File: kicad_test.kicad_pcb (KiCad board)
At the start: 2 copper layers, 10 parts, among them U1 ICM7555xP, U2 ICM7555xP

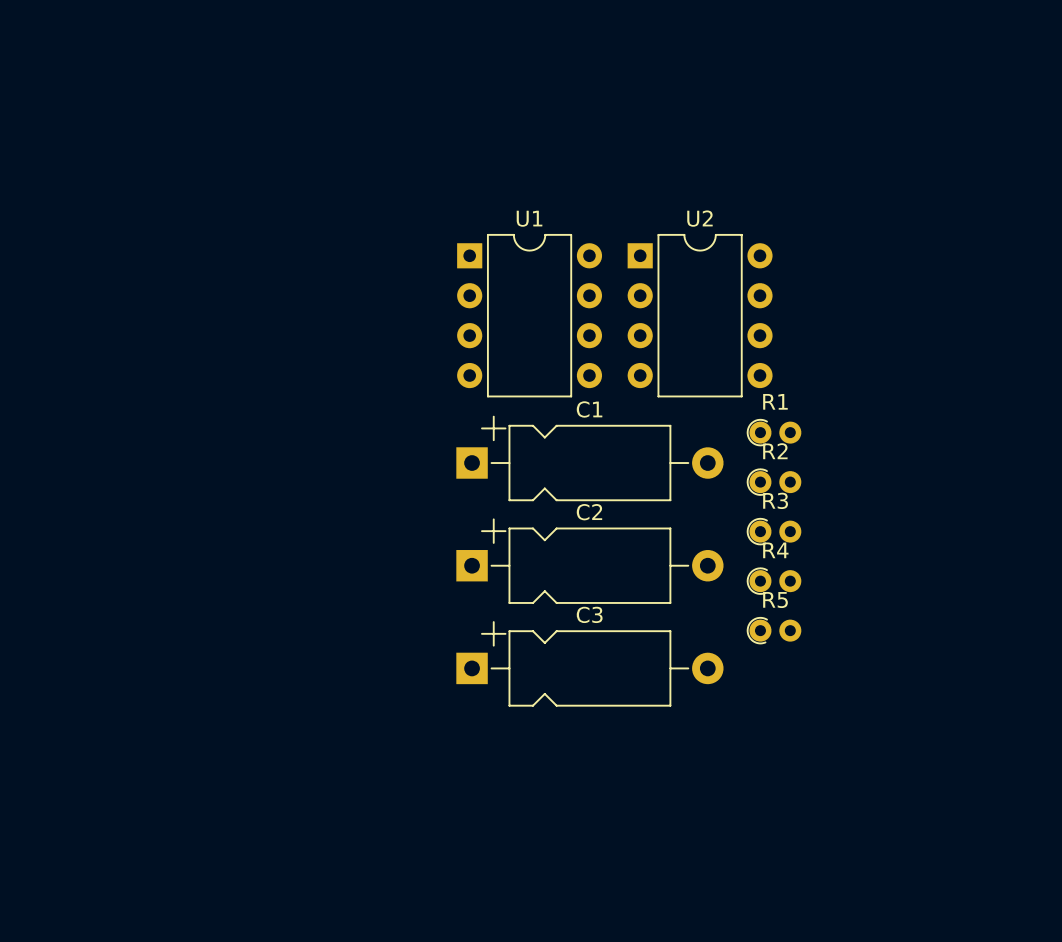
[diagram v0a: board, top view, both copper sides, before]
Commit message: moving parts in pcb
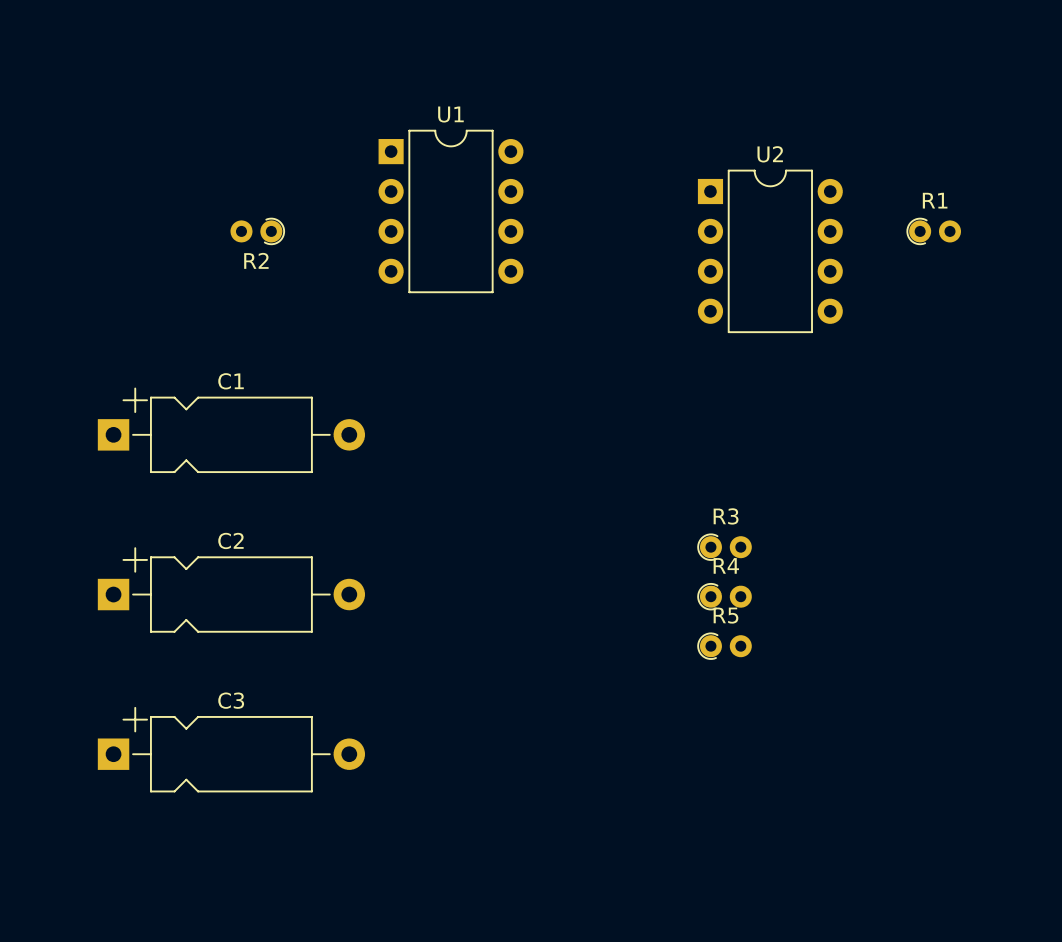
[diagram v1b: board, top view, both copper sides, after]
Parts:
- moved R2 35.0 mm to (45.7, 55.9), turned to 180 degrees
- moved C3 23.5 mm to (35.7, 89.1)
- moved C2 22.9 mm to (35.7, 79.0)
- moved C1 22.9 mm to (35.7, 68.8)
- moved R1 16.3 mm to (87.0, 55.9)
- moved U1 8.30 mm to (53.3, 50.8)
- moved U2 6.06 mm to (73.7, 53.3)
- moved R4 3.30 mm to (73.7, 79.1)
- moved R3 3.30 mm to (73.7, 76.0)
- moved R5 3.30 mm to (73.7, 82.3)
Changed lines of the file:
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@@
 	(footprint "Resistor_THT:R_Axial_DIN0204_L3.6mm_D1.6mm_P1.90mm_Vertical"
 		(layer "F.Cu")
-		(at 76.84 78.13)
+		(at 73.69 79.12)
 		(descr "Resistor, Axial_DIN0204 series, Axial, Vertical, pin pitch=1.9mm, 0.167W, length*diameter=3.6*1.6mm^2, http://cdn-reichelt.de/documents/datenblatt/B400/1_4W%23YAG.pdf")
 		(tags "Resistor Axial_DIN0204 series Axial Vertical pin pitch 1.9mm 0.167W length 3.6mm diameter 1.6mm")
@@
 	(footprint "Package_DIP:DIP-8_W7.62mm"
 		(layer "F.Cu")
-		(at 58.34 57.43)
+		(at 53.34 50.8)
 		(descr "8-lead though-hole mounted DIP package, row spacing 7.62 mm (300 mils)")
 		(tags "THT DIP DIL PDIP 2.54mm 7.62mm 300mil")
@@
 	(footprint "Resistor_THT:R_Axial_DIN0204_L3.6mm_D1.6mm_P1.90mm_Vertical"
 		(layer "F.Cu")
-		(at 76.84 81.28)
+		(at 73.69 82.27)
 		(descr "Resistor, Axial_DIN0204 series, Axial, Vertical, pin pitch=1.9mm, 0.167W, length*diameter=3.6*1.6mm^2, http://cdn-reichelt.de/documents/datenblatt/B400/1_4W%23YAG.pdf")
 		(tags "Resistor Axial_DIN0204 series Axial Vertical pin pitch 1.9mm 0.167W length 3.6mm diameter 1.6mm")
@@
 	(footprint "Resistor_THT:R_Axial_DIN0204_L3.6mm_D1.6mm_P1.90mm_Vertical"
 		(layer "F.Cu")
-		(at 76.84 68.68)
+		(at 87 55.88)
 		(descr "Resistor, Axial_DIN0204 series, Axial, Vertical, pin pitch=1.9mm, 0.167W, length*diameter=3.6*1.6mm^2, http://cdn-reichelt.de/documents/datenblatt/B400/1_4W%23YAG.pdf")
 		(tags "Resistor Axial_DIN0204 series Axial Vertical pin pitch 1.9mm 0.167W length 3.6mm diameter 1.6mm")
@@
 	(footprint "Capacitor_THT:CP_Axial_L10.0mm_D4.5mm_P15.00mm_Horizontal"
 		(layer "F.Cu")
-		(at 58.49 70.615)
+		(at 35.68 68.8225)
 		(descr "CP, Axial series, Axial, Horizontal, pin pitch=15mm, , length*diameter=10*4.5mm^2, Electrolytic Capacitor, , http://www.vishay.com/docs/28325/021asm.pdf")
 		(tags "CP Axial series Axial Horizontal pin pitch 15mm  length 10mm diameter 4.5mm Electrolytic Capacitor")
@@
 	(footprint "Resistor_THT:R_Axial_DIN0204_L3.6mm_D1.6mm_P1.90mm_Vertical"
 		(layer "F.Cu")
-		(at 76.84 71.83)
+		(at 45.72 55.88 180)
 		(descr "Resistor, Axial_DIN0204 series, Axial, Vertical, pin pitch=1.9mm, 0.167W, length*diameter=3.6*1.6mm^2, http://cdn-reichelt.de/documents/datenblatt/B400/1_4W%23YAG.pdf")
 		(tags "Resistor Axial_DIN0204 series Axial Vertical pin pitch 1.9mm 0.167W length 3.6mm diameter 1.6mm")
 		(property "Reference" "R2"
-			(at 0.95 -1.92 0)
+			(at 0.95 -1.92 360)
 			(layer "F.SilkS")
 			(effects
@@
 		)
 		(property "Value" "R_US"
-			(at 0.95 1.92 0)
+			(at 0.95 1.92 360)
 			(layer "F.Fab")
 			(effects
@@
 		)
 		(property "Footprint" "Resistor_THT:R_Axial_DIN0204_L3.6mm_D1.6mm_P1.90mm_Vertical"
-			(at 0 0 0)
+			(at 0 0 180)
 			(unlocked yes)
 			(layer "F.Fab")
@@
 		)
 		(property "Datasheet" ""
-			(at 0 0 0)
+			(at 0 0 180)
 			(unlocked yes)
 			(layer "F.Fab")
@@
 		)
 		(property "Description" "Resistor, US symbol"
-			(at 0 0 0)
+			(at 0 0 180)
 			(unlocked yes)
 			(layer "F.Fab")
@@
 		)
 		(fp_line
+			(start 2.86 1.05)
+			(end 2.86 -1.05)
+			(stroke
+				(width 0.05)
+				(type solid)
+			)
+			(layer "F.CrtYd")
+		)
+		(fp_line
+			(start 2.86 -1.05)
+			(end -1.05 -1.05)
+			(stroke
+				(width 0.05)
+				(type solid)
+			)
+			(layer "F.CrtYd")
+		)
+		(fp_line
+			(start -1.05 1.05)
+			(end 2.86 1.05)
+			(stroke
+				(width 0.05)
+				(type solid)
+			)
+			(layer "F.CrtYd")
+		)
+		(fp_line
 			(start -1.05 -1.05)
 			(end -1.05 1.05)
-			(stroke
-				(width 0.05)
-				(type solid)
-			)
-			(layer "F.CrtYd")
-		)
-		(fp_line
-			(start -1.05 1.05)
-			(end 2.86 1.05)
-			(stroke
-				(width 0.05)
-				(type solid)
-			)
-			(layer "F.CrtYd")
-		)
-		(fp_line
-			(start 2.86 -1.05)
-			(end -1.05 -1.05)
-			(stroke
-				(width 0.05)
-				(type solid)
-			)
-			(layer "F.CrtYd")
-		)
-		(fp_line
-			(start 2.86 1.05)
-			(end 2.86 -1.05)
 			(stroke
 				(width 0.05)
@@
 		)
 		(fp_text user "${REFERENCE}"
-			(at 0.95 -1.92 0)
+			(at 0.95 -1.92 360)
 			(layer "F.Fab")
 			(effects
@@
 		)
 		(pad "1" thru_hole circle
-			(at 0 0)
+			(at 0 0 180)
 			(size 1.4 1.4)
 			(drill 0.7)
@@
 		)
 		(pad "2" thru_hole oval
-			(at 1.9 0)
+			(at 1.9 0 180)
 			(size 1.4 1.4)
 			(drill 0.7)
@@
 	(footprint "Resistor_THT:R_Axial_DIN0204_L3.6mm_D1.6mm_P1.90mm_Vertical"
 		(layer "F.Cu")
-		(at 76.84 74.98)
+		(at 73.69 75.97)
 		(descr "Resistor, Axial_DIN0204 series, Axial, Vertical, pin pitch=1.9mm, 0.167W, length*diameter=3.6*1.6mm^2, http://cdn-reichelt.de/documents/datenblatt/B400/1_4W%23YAG.pdf")
 		(tags "Resistor Axial_DIN0204 series Axial Vertical pin pitch 1.9mm 0.167W length 3.6mm diameter 1.6mm")
@@
 	(footprint "Capacitor_THT:CP_Axial_L10.0mm_D4.5mm_P15.00mm_Horizontal"
 		(layer "F.Cu")
-		(at 58.49 77.15)
+		(at 35.68 78.9825)
 		(descr "CP, Axial series, Axial, Horizontal, pin pitch=15mm, , length*diameter=10*4.5mm^2, Electrolytic Capacitor, , http://www.vishay.com/docs/28325/021asm.pdf")
 		(tags "CP Axial series Axial Horizontal pin pitch 15mm  length 10mm diameter 4.5mm Electrolytic Capacitor")
@@
 	(footprint "Capacitor_THT:CP_Axial_L10.0mm_D4.5mm_P15.00mm_Horizontal"
 		(layer "F.Cu")
-		(at 58.49 83.685)
+		(at 35.68 89.1425)
 		(descr "CP, Axial series, Axial, Horizontal, pin pitch=15mm, , length*diameter=10*4.5mm^2, Electrolytic Capacitor, , http://www.vishay.com/docs/28325/021asm.pdf")
 		(tags "CP Axial series Axial Horizontal pin pitch 15mm  length 10mm diameter 4.5mm Electrolytic Capacitor")
@@
 	(footprint "Package_DIP:DIP-8_W7.62mm"
 		(layer "F.Cu")
-		(at 69.19 57.43)
+		(at 73.66 53.34)
 		(descr "8-lead though-hole mounted DIP package, row spacing 7.62 mm (300 mils)")
 		(tags "THT DIP DIL PDIP 2.54mm 7.62mm 300mil")

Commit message: adding edge cut rect
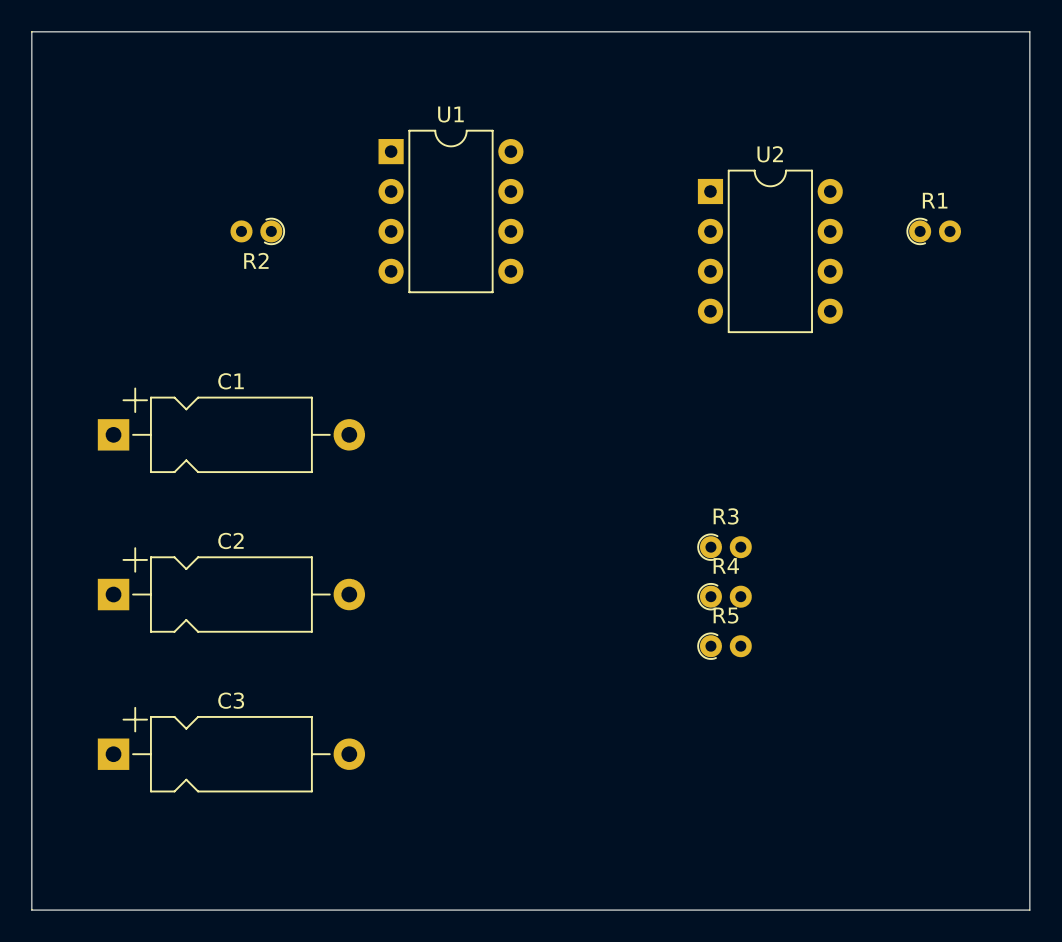
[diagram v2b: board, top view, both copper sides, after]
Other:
- board outline added: 63.5 x 55.9 mm
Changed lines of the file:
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@@
 		)
 	)
+	(gr_rect
+		(start 30.48 43.18)
+		(end 93.98 99.06)
+		(stroke
+			(width 0.05)
+			(type default)
+		)
+		(fill none)
+		(layer "Edge.Cuts")
+	)
 )

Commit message: adding first traces
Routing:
- net Net-(U1-TR): track 0.00 -> 30.5 mm
- net Net-(U1-CV): track 0.00 -> 21.4 mm
- net Net-(U1-Q): track 0.00 -> 7.62 mm
- net Net-(U2-DIS): track 0.00 -> 5.72 mm
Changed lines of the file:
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@@
 		(layer "Edge.Cuts")
 	)
+	(segment
+		(start 73.66 60.96)
+		(end 81.28 60.96)
+		(width 0.2)
+		(layer "F.Cu")
+		(net 1)
+	)
+	(segment
+		(start 60.96 58.42)
+		(end 63.5 58.42)
+		(width 0.2)
+		(layer "F.Cu")
+		(net 1)
+	)
+	(segment
+		(start 63.5 58.42)
+		(end 66.04 60.96)
+		(width 0.2)
+		(layer "F.Cu")
+		(net 1)
+	)
+	(segment
+		(start 66.04 60.96)
+		(end 73.66 60.96)
+		(width 0.2)
+		(layer "F.Cu")
+		(net 1)
+	)
+	(segment
+		(start 81.28 55.88)
+		(end 87 55.88)
+		(width 0.2)
+		(layer "F.Cu")
+		(net 5)
+	)
+	(segment
+		(start 45.72 55.88)
+		(end 53.34 55.88)
+		(width 0.2)
+		(layer "F.Cu")
+		(net 8)
+	)
+	(segment
+		(start 63.5 48.26)
+		(end 73.66 58.42)
+		(width 0.2)
+		(layer "F.Cu")
+		(net 16)
+	)
+	(segment
+		(start 53.34 53.34)
+		(end 52.24 52.24)
+		(width 0.2)
+		(layer "F.Cu")
+		(net 16)
+	)
+	(segment
+		(start 52.24 52.24)
+		(end 52.24 49.36)
+		(width 0.2)
+		(layer "F.Cu")
+		(net 16)
+	)
+	(segment
+		(start 53.34 48.26)
+		(end 63.5 48.26)
+		(width 0.2)
+		(layer "F.Cu")
+		(net 16)
+	)
+	(segment
+		(start 52.24 49.36)
+		(end 53.34 48.26)
+		(width 0.2)
+		(layer "F.Cu")
+		(net 16)
+	)
 )

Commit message: adding two-point trace
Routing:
- net GNDREF: track 0.00 -> 10.2 mm
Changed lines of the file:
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@@
 		(tags "Resistor Axial_DIN0204 series Axial Vertical pin pitch 1.9mm 0.167W length 3.6mm diameter 1.6mm")
 		(property "Reference" "R2"
-			(at 0.95 -1.92 360)
+			(at 0.95 -1.92 0)
 			(layer "F.SilkS")
 			(effects
@@
 		)
 		(property "Value" "R_US"
-			(at 0.95 1.92 360)
+			(at 0.95 1.92 0)
 			(layer "F.Fab")
 			(effects
@@
 		)
 		(fp_text user "${REFERENCE}"
-			(at 0.95 -1.92 360)
+			(at 0.95 -1.92 0)
 			(layer "F.Fab")
 			(effects
@@
 	)
 	(segment
+		(start 50.68 68.8225)
+		(end 50.68 78.9825)
+		(width 0.2)
+		(layer "F.Cu")
+		(net 2)
+	)
+	(segment

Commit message: add and remove trace
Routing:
- net Net-(U1-CV): track 21.4 -> 45.9 mm
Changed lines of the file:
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@@
-	)
-	(segment
-		(start 73.66 60.96)
-		(end 81.28 60.96)
-		(width 0.2)
-		(layer "F.Cu")
-		(net 1)
 	)
 	(segment
@@
 	)
 	(segment
+		(start 46.0825 58.42)
+		(end 35.68 68.8225)
+		(width 0.2)
+		(layer "F.Cu")
+		(net 1)
+	)
+	(segment
 		(start 66.04 60.96)
 		(end 73.66 60.96)
 		(width 0.2)
 		(layer "F.Cu")
+		(net 1)
+	)
+	(segment
+		(start 53.34 58.42)
+		(end 46.0825 58.42)
+		(width 0.2)
+		(layer "F.Cu")
+		(net 1)
+	)
+	(segment
+		(start 35.68 68.8225)
+		(end 35.68 78.9825)
+		(width 0.2)
+		(layer "F.Cu")

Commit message: updating to KiCAD 9
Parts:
- removed R5: R, Resistor_THT:R_Axial_DIN0204_L3.6mm_D1.6mm_P1.90mm_Vertical
- added C4: C, Capacitor_THT:CP_Axial_L10.0mm_D4.5mm_P15.00mm_Horizontal, F.Cu at (66.3, 86.4)
- R3: value 220 -> 100k; footprint Resistor_THT:R_Axial_DIN0204_L3.6mm_D1.6mm_P1.90mm_Vertical -> Resistor_THT:R_Axial_DIN0411_L9.9mm_D3.6mm_P12.70mm_Horizontal
